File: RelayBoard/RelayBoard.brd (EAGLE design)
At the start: 100 x 100 mm, 95 parts, among them IC1 MCP2551/SN RSC 402-904, IC2 MCP2515-I/SOGRB2 RSC 628-3548, U1 CD74HC4067SM96, U2 LM1084IS-3.3, U3 CD74HC4067SM96, U4 ADS1115IDGST, U6 LM1084IS-3.3, U7 LM1084IS-3.3, X1 332-50, X2 332-46

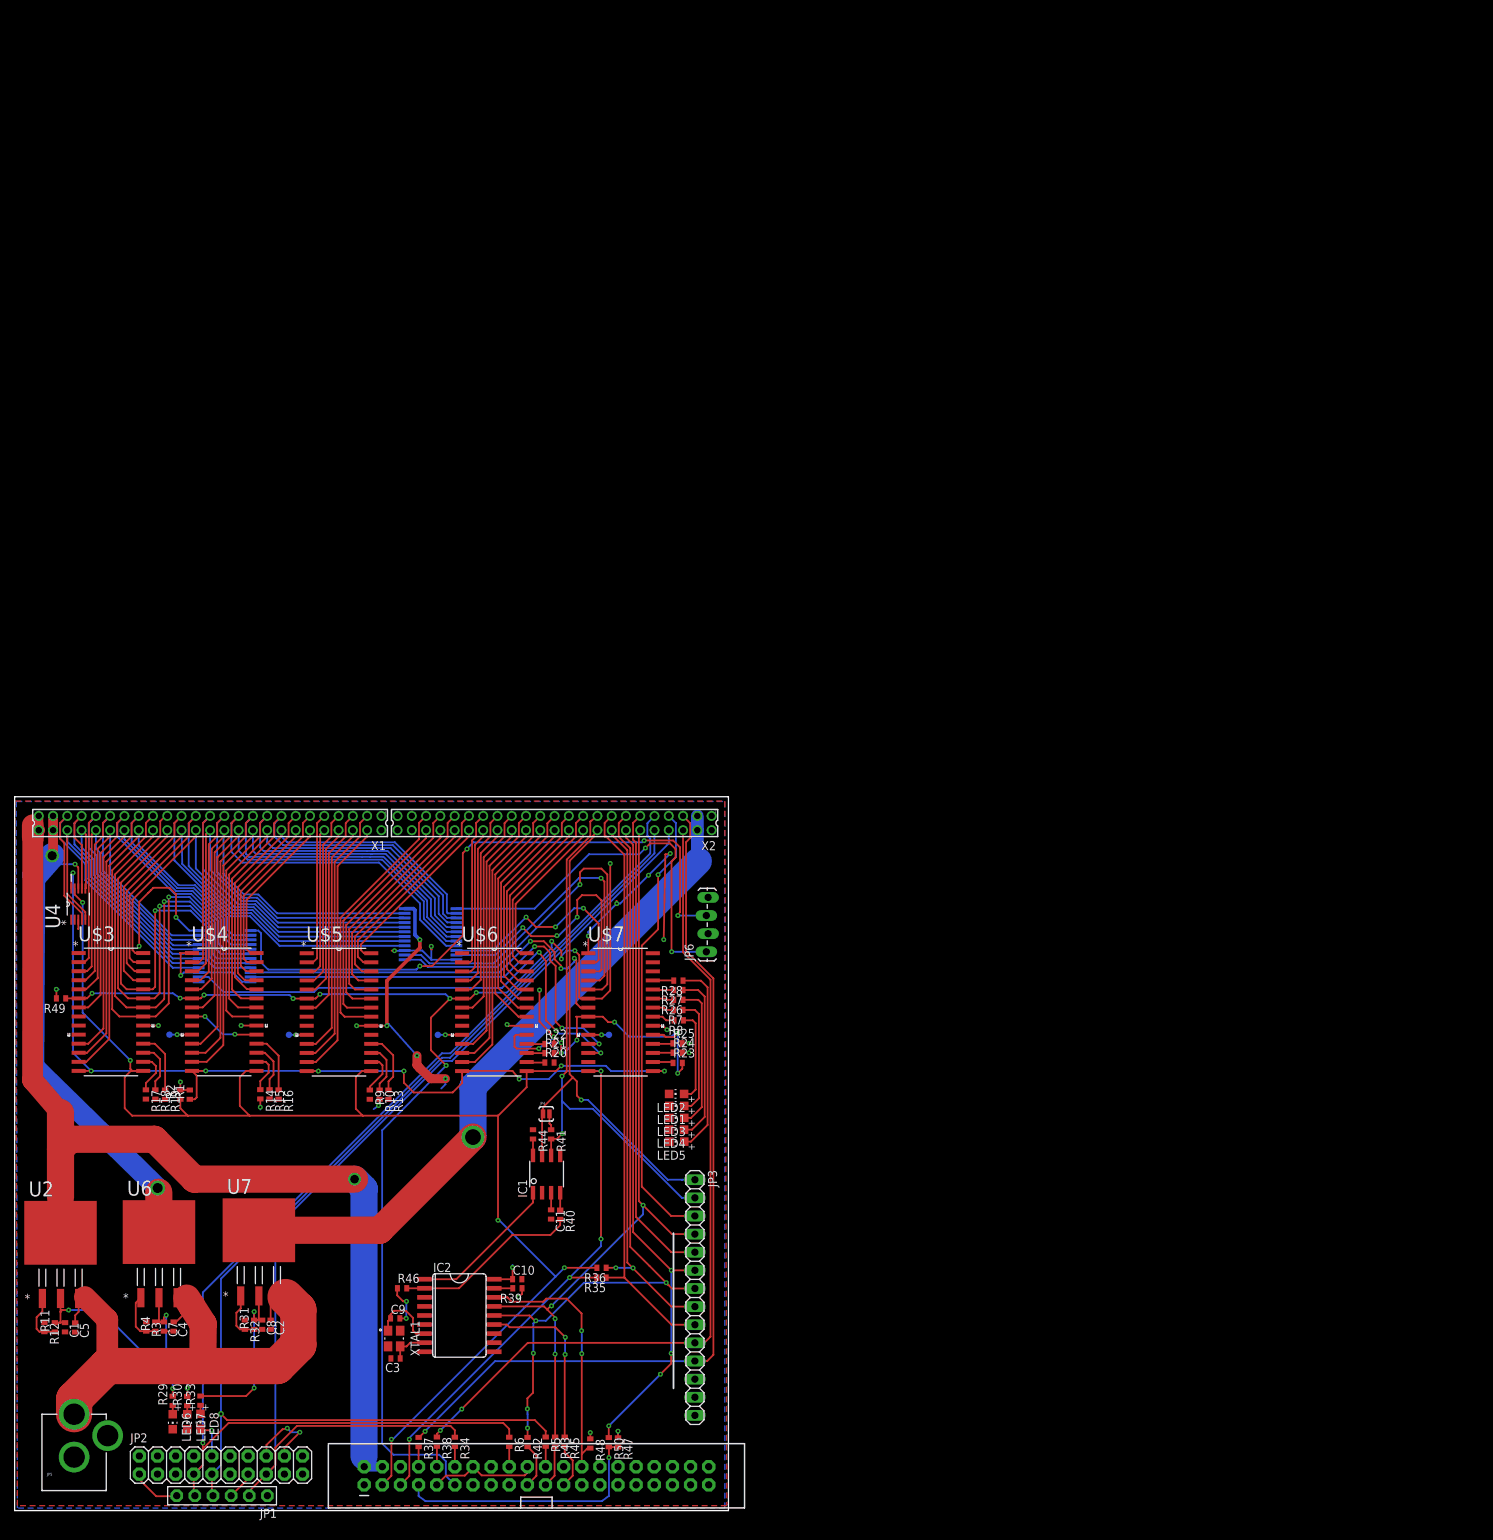
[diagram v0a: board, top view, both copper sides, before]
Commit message: remove: - ioexpanders add:       - tm4c129 mcu                - plus two multiplexer and two BNC connector                - 139x115mm board size
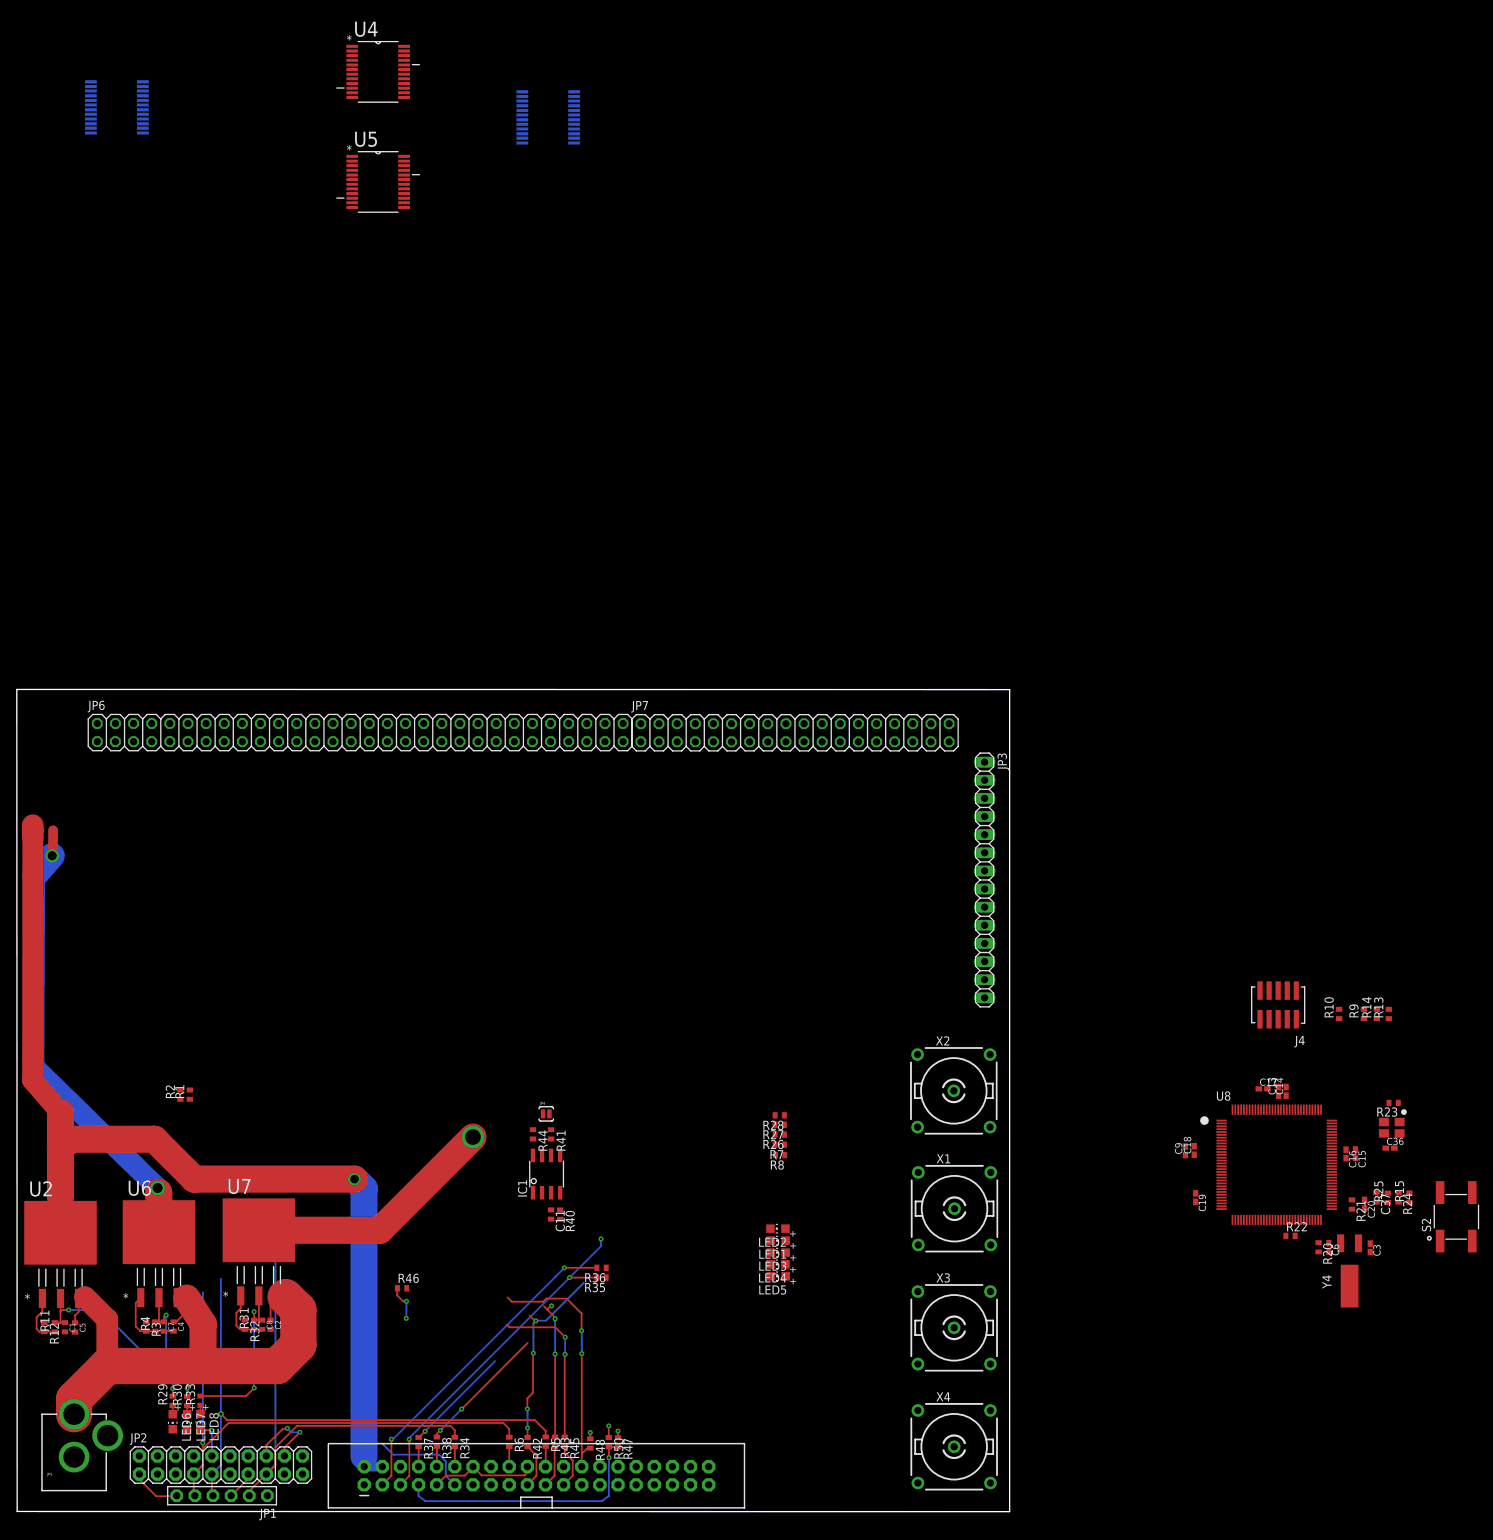
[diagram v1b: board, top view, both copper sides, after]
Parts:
- removed C10: 100nF, eagle-ltspice:C0402
- removed IC2: MCP2515-I/SOGRB2 RSC 628-3548, mcp2515:SO18L
- removed R16, R17, R18, R19: (no value), resistor:R0402
- removed R39: 4k7, resistor:R0402
- removed R49: 10k, resistor:R0402
- removed TP1, TP2, TP3, TP4: TPTP09R, testpad:TP09R
- removed U$3, U$4, U$5, U$6, U$7: MCP23016-I/SO, Port Expander:SOIC127P1030X265-28N
- removed XTAL1: 7M-16.000MAAJ-T, TXC-7M-16.000MAAJ-T:TXC_7M-16.000MAAJ-T
- added C13, C14, C16, C17, C18, C19, C20: 0.1uF, rcl:C0402K
- added C15: 2.2uF, rcl:C0402K
- added C36, C6: 12pF, rcl:C0402K
- added C37: 0.1uF, eagle-ltspice:C0402
- added J4: JTAG_ARM_10PIN, MRDT-Connectors:CON_2X5_50MIL
- added JP7: (no value), pinhead:2X18
- added S2: SWITCH_TACTILE, MRDT-UserInput:SWITCH_6MM_6MM_TE_CON_SMD
- added U5: CD74HC4067SM96, MUX:SOP65P780X200-24N
- added U8: TM4C1294NCPDT, MRDT-Microcontrollers:TQFP-128
- added X3, X4: A1944-50, con-coax:A1944
- added Y3: NX3225GA, MRDT-Passives:NDK3.2X2.5
- added Y4: CRYATL_32K_SMD, MRDT-Passives:CRYSTAL_32K_SMD
- C3, C9: value 22pF -> 12pF; device eagle-ltspice:C0402 -> rcl:C0402K
- JP6: device SparkFun-Connectors:1X04_LOCK_LONGPADS -> pinhead:2X30
- R1, R11, R12, R2, R26, R27, R28, R29, R3, R30, R31, R32, R33, R34, R35, R36, R37, R38, R4, R40, R41, R42, R43, R44, R45, R46, R47, R48, R5, R50, R6, R7, R8: device resistor:R0402 -> resistor:R0402@1
- R10, R13, R14, R15, R9: value (none) -> 4.7k; device resistor:R0402 -> resistor:R0402@1
- R20: value (none) -> 1M; device resistor:R0402 -> rcl:R0402
- R21: value (none) -> 51; device resistor:R0402 -> rcl:R0402
- R22: value (none) -> 4.87k 1%; device resistor:R0402 -> rcl:R0402
- R23: value (none) -> 2k; device resistor:R0402 -> rcl:R0402
- R24: value (none) -> 100; device resistor:R0402 -> rcl:R0402
- R25: value (none) -> 10k; device resistor:R0402 -> rcl:R0402
- U4: value ADS1115IDGST -> CD74HC4067SM96; device ADC:SOP50P490X110-10N -> MUX:SOP65P780X200-24N
- X1: value 332-50 -> A1944-50; device con-garry:332-50 -> con-coax:A1944
- X2: value 332-46 -> A1944-50; device con-garry:332-46 -> con-coax:A1944
- moved R15 160.3 mm to (195.4, 43.8), turned to 90 degrees
- moved R14 156.8 mm to (190.8, 69.6), turned to 90 degrees
- moved R13 140.6 mm to (192.5, 69.6), turned to 90 degrees
- moved R9 139.7 mm to (189.0, 69.6), turned to 90 degrees
- moved C3 137.4 mm to (189.9, 36.8), turned to 270 degrees
- moved R10 134.9 mm to (185.5, 69.6), turned to 90 degrees
- moved U4 123.9 mm to (50.9, 201.5), turned to 0 degrees
- moved U3 119.9 mm to (14.3, 196.6)
- moved X1 117.5 mm to (131.7, 42.3), turned to 0 degrees
- moved U1 115.6 mm to (74.8, 195.2)
- moved R21 114.4 mm to (187.4, 42.9), turned to 270 degrees
- moved C9 113.2 mm to (164.0, 50.4), turned to 90 degrees
- moved R20 110.8 mm to (182.7, 36.9), turned to 270 degrees
- moved R22 107.2 mm to (178.7, 38.5)
- moved R24 103.0 mm to (193.9, 43.9), turned to 270 degrees
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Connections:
- removed net CAN_INT: IC2.12
- removed net D28: U$4.26, X1.14
- removed net D29: U$4.25, X1.13
- removed net D30: U$4.28, X1.12
- removed net D31: U$4.27, X1.11
- removed net D32: U$5.3, X1.10
- removed net D33: U$5.2, X1.9
- removed net D34: U$5.5, X1.8
- removed net D35: U$5.4, X1.7
- removed net D36: U$5.11, X1.6
- removed net D37: U$5.7, X1.5
- removed net D38: U$5.13, X1.4
- removed net D39: U$5.12, X1.3
- removed net D40: U$5.22, X2.42
- removed net D41: U$5.21, X2.41
- removed net D42: U$5.24, X2.40
- removed net D43: U$5.23, X2.39
- removed net D44: U$5.26, X2.38
- removed net D45: U$5.25, X2.37
- removed net D46: U$5.28, X2.36
- removed net D47: U$5.27, X2.35
- removed net D48: U$6.3, X2.34
- removed net D49: U$6.2, X2.33
- removed net D50: U$6.5, X2.32
- removed net D51: U$6.4, X2.31
- removed net D52: U$6.11, X2.30
- removed net D53: U$6.7, X2.29
- removed net D54: U$6.13, X2.28
- removed net D55: U$6.12, X2.27
- removed net D56: U$6.22, X2.26
- removed net D57: U$6.21, X2.25
- removed net D58: U$6.24, X2.24
- removed net D59: U$6.23, X2.23
- removed net D60: U$6.26, X2.22
- removed net D61: U$6.25, X2.21
- removed net D62: U$6.28, X2.20
- removed net D63: U$6.27, X2.19
- removed net M2S03: U$7.13
- removed net N$10: C9.1, IC2.7, XTAL1.1
- removed net N$11: R16.1, U$4.18
- removed net N$12: R23.1, U$7.16
- removed net N$13: R24.1, U$7.17
- removed net N$14: R25.1, U$7.18
- removed net N$15: R20.1, U$6.16
- removed net N$16: R21.1, U$6.17
- removed net N$17: R22.1, U$6.18
- removed net N$21: R9.1, U$5.16
- removed net N$22: R10.1, U$5.17
- removed net N$24: R13.1, U$5.18
- removed net N$26: R17.1, U$3.16
- removed net N$27: R18.1, U$3.17
- removed net N$28: R19.1, U$3.18
- removed net N$37: U$3.10
- removed net N$38: TP1.TP, U$6.10
- removed net N$39: U$7.26
- removed net N$4: R14.1, U$4.16
- removed net N$40: U$7.27
- removed net N$41: U$7.28
- removed net N$49: IC2.17, R39.2
- removed net N$6: R15.1, U$4.17
- removed net N$7: TP3.TP, U$5.10
- removed net N$8: TP4.TP, U$4.10
- removed net N$9: C3.1, IC2.8, XTAL1.3
- new net !RESET: J4.P10, R15.1, R24.2, S2.P$3, S2.P$4
- new net +3V3: C16.1, C17.1, C18.1, C19.1, J4.P1, R20.2, R21.2, R25.1, U8.P$101, U8.P$113, U8.P$122, U8.P$16, U8.P$26, U8.P$28, U8.P$39, U8.P$47, U8.P$51, U8.P$52, U8.P$69, U8.P$7, U8.P$79, U8.P$8, U8.P$9, U8.P$90
- new net EN0LED0: U8.P$42
- new net EN0LED1: U8.P$46
- new net EN0RXI_N: U8.P$53
- new net EN0RXI_P: U8.P$54
- new net EN0TXO_N: U8.P$56
- new net EN0TXO_P: U8.P$57
- new net N_$2: C20.1, R21.1, U8.P$68
- new net N_$24: R20.1, U8.P$64
- new net N_$28: C13.1, C14.1, C15.1, U8.P$115, U8.P$87
- new net N_$29: R22.2, U8.P$59
- new net N_$30: R23.2, U8.P$89
- new net N_$31: C36.1, U8.P$88, Y3.P$3
- new net N_$32: C9.1, R23.1, Y3.P$1
- new net N_$33: C37.1, R24.1, R25.2, U8.P$70
- new net N_$34: C6.1, U8.P$66, Y4.P$1
- new net N_$35: C3.1, U8.P$67, Y4.P$2
- new net TARGET_TCK/SWCLK: J4.P4, R10.1, U8.P$100
- new net TARGET_TDI: J4.P8, R14.1, U8.P$98
- new net TARGET_TDO/SWO: J4.P6, R13.1, U8.P$97
- new net TARGET_TMS/SWDIO: J4.P2, R9.1, U8.P$99
- net 3.6V: no longer X2.3, X2.4
- net 5V: no longer X1.49, X1.50
- net A0: now also U5.17; no longer U4.5, X1.46
- net A1: now also U5.16; no longer U4.4, X1.45
- net A2: now also U5.19; no longer U4.6, X1.44
- net A3: now also U5.18; no longer U4.7, X1.43
- net CAN_CS: no longer IC2.16
- net CAN_N: no longer X2.17
- net CAN_P: no longer X2.18
- net CS: no longer X2.14
- net D0: now also U5.21; no longer U$3.3, X1.42
- net D1: now also U5.20; no longer U$3.2, X1.41
- net D10: now also U5.9; no longer U$3.24, X1.32
- net D11: now also U5.8; no longer U$3.23, X1.31
- net D12: now also U4.17; no longer U$3.26, X1.30
- net D13: now also U4.16; no longer U$3.25, X1.29
- net D14: now also U4.19; no longer U$3.28, X1.28
- net D15: now also U4.18; no longer U$3.27, X1.27
- net D16: now also U4.21; no longer U$4.3, X1.26
- net D17: now also U4.20; no longer U$4.2, X1.25
- net D18: now also U4.23; no longer U$4.5, X1.24
- net D19: now also U4.22; no longer U$4.4, X1.23
- net D2: now also U5.23; no longer U$3.5, X1.40
- net D20: now also U4.8; no longer U$4.11, X1.22
- net D21: now also U4.9; no longer U$4.7, X1.21
- net D22: now also U4.6; no longer U$4.13, X1.20
- net D23: now also U4.7; no longer U$4.12, X1.19
- net D24: now also U4.4; no longer U$4.22, X1.18
- net D25: now also U4.5; no longer U$4.21, X1.17
- net D26: now also U4.2; no longer U$4.24, X1.16
- net D27: now also U4.3; no longer U$4.23, X1.15
- net D3: now also U5.22; no longer U$3.4, X1.39
- net D4: now also U5.4; no longer U$3.11, X1.38
- net D5: now also U5.5; no longer U$3.7, X1.37
- net D6: now also U5.2; no longer U$3.13, X1.36
- net D7: now also U5.3; no longer U$3.12, X1.35
- net D8: now also U5.7; no longer U$3.22, X1.34
- net D9: now also U5.6; no longer U$3.21, X1.33
- net DUT_CONNECT: no longer U$7.24
- net GND: now also C13.2, C14.2, C15.2, C16.2, C17.2, C18.2, C19.2, C20.2, C36.2, C37.2, C6.2, J4.P3, J4.P5, R22.1, S2.P$1, S2.P$2, U4.12, U4.15, U5.12, U5.15, U8.P$10, U8.P$114, U8.P$17, U8.P$48, U8.P$55, U8.P$58, U8.P$80, X1.3, X1.4, X1.5, X2.3, X2.4, X2.5, X3.2, X3.3, X3.4, X3.5, X4.2, X4.3, X4.4, X4.5; no longer C10.2, IC2.9, JP6.2, JP6.4, R13.2, R15.2, R16.2, R17.2, R18.2, R19.2, R20.2, R21.2, R23.2, R9.2, U$3.1, U$3.19, U$3.8, U$4.1, U$4.19, U$4.8, U$5.1, U$5.19, U$5.8, U$6.1, U$6.19, U$6.8, U$7.1, U$7.19, U$7.8, U4.1, U4.3, X1.1, X2.1, X2.45, X2.46
- net IO_INT: no longer R49.1, U$3.6, U$4.6, U$5.6, U$6.6, U$7.6
- net M1OUT: now also U4.1, X1.1; no longer JP6.1
- net M1S0: now also U4.10; no longer U$7.2
- net M1S1: now also U4.11; no longer U$7.3
- net M1S2: now also U4.14; no longer U$7.4
- net M1S3: now also U4.13; no longer U$7.5
- net M2OUT: now also U5.1, X2.1; no longer JP6.3
- net M2S0: now also U5.10; no longer U$7.7
- net M2S1: now also U5.11; no longer U$7.11
- net M2S2: now also U5.14; no longer U$7.12
- net M2S3: now also U5.13
- net MISO: no longer IC2.15, X2.12
- net MOSI: no longer IC2.14, X2.13
- net N$2: now also R10.2, R13.2, R14.2, R15.2, R9.2; no longer TP2.TP, U$7.10
- net N$45: no longer IC2.2
- net N$47: no longer IC2.1
- net NRESET: no longer X2.8
- net ONEWIRE: no longer X2.7
- net PROGRAM: no longer U$7.25
- net RX: now also J4.P7, U8.P$33; no longer X2.6
- net SCK: no longer IC2.13
- net SCL: no longer X2.15
- net SCLK: no longer X2.11
- net SDA: no longer X2.16
- net SWDCLK: no longer X2.10
- net SWDIO: no longer X2.9
- net TEST_FAIL: no longer U$7.23
- net TEST_PASS: no longer U$7.22
- net TEST_RUN: no longer U$7.21
- net TFT_SCL: no longer U$3.14, U$4.14, U$5.14, U$6.14, U$7.14, U4.10
- net TFT_SDA: no longer U$3.15, U$4.15, U$5.15, U$6.15, U$7.15, U4.9
- net TX: now also J4.P9, U8.P$34; no longer X2.5
- net VCC: now also U4.24, U5.24; no longer C10.1, IC2.18, R10.2, R14.2, R22.2, R24.2, R25.2, R39.1, R49.2, U$3.20, U$4.20, U$5.20, U$6.20, U$7.20, U4.8, X1.47, X1.48
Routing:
- net IO_INT: track 190.3 -> 13.8 mm, vias 12 -> 0
- net TFT_SDA: track 209.9 -> 45.6 mm, vias 7 -> 2
- net TFT_SCL: track 193.8 -> 49.9 mm, vias 10 -> 3
- net GND: track 159.0 -> 38.6 mm, vias 22 -> 5
- net TX: track 123.8 -> 15.2 mm
- net VCC: track 194.9 -> 93.9 mm, vias 28 -> 6
- net RX: track 117.0 -> 18.5 mm
- net SWDIO: track 170.8 -> 76.8 mm
- net M2OUT: track 93.1 -> 0.00 mm, vias 4 -> 0
- net CS: track 94.6 -> 1.64 mm, vias 4 -> 1
- net MOSI: track 116.8 -> 27.0 mm, vias 5 -> 4
- net SWDCLK: track 167.0 -> 78.3 mm
- net MISO: track 107.9 -> 19.8 mm, vias 4 -> 3
- net SCL: track 81.5 -> 0.00 mm
- net NRESET: track 150.2 -> 70.8 mm
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- removed copper zone on layer 1, net GND
- removed copper zone on layer 16, net VCC
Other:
- board size 100 x 100 mm -> 139.1 x 115.2 mm
